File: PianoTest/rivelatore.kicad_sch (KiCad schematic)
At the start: 47 parts, among them J101 SMA preampl., J102 SMA shaper, Q101 BF862, Q102 BF862, U101 OPA4172ID, U102 ADS8326IDGKT, U103 TMP117AIDRVR

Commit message: PianoTest: discriminatore, latch e rilevatore di picco
Comparatore TLV3501 su SHAPER_OUT con soglia dal canale B del DAC61402
(partitore 22k/10k, BAT54S), latch 74LVC1G74 su GPA7 dell'MCP (ALERT#),
uscita HIT su TP e SMA. Rilevatore di picco OPA2365 + BAS416 + hold 1 nF
C0G prima dell'ADS8326, con reset da accesso SPI all'indirizzo 3 e
ponticello 0R per scavalcarlo. Trigger del LED dallo strobe dell'indirizzo 4.
Articolo: sezione 3.1 (formatore e acquisizione) aggiornata e ricompilata.
ERC 0.

Co-Authored-By: Claude Opus 5.5 (1M context) <noreply@anthropic.com>
Claude-Session: https://claude.ai/code/session_01J3krgWFTUEjwvCnwUp9cQn
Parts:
- added C108: 1nF C0G, Capacitor_SMD:C_0603_1608Metric, symbol Device:C
- added C118, C119, C120: 100nF, Capacitor_SMD:C_0603_1608Metric, symbol Device:C
- added D102, D103: BAS416, Diode_SMD:D_SOD-323, symbol Device:D
- added J103: SMA HIT, Connector_Coaxial:SMA_Amphenol_132134_Vertical, symbol Connector:Conn_Coaxial
- added Q103: BSS138, Package_TO_SOT_SMD:SOT-23, symbol PianoTest:BSS138
- added R130, R132: 1k, Resistor_SMD:R_0603_1608Metric, symbol Device:R
- added R131: 1M, Resistor_SMD:R_0603_1608Metric, symbol Device:R
- added R133: 10k, Resistor_SMD:R_0603_1608Metric, symbol Device:R
- added R134: 100k, Resistor_SMD:R_0603_1608Metric, symbol Device:R
- added R135, R136: 0R, Resistor_SMD:R_0603_1608Metric, symbol Device:R
- added R137: 100R, Resistor_SMD:R_0603_1608Metric, symbol Device:R
- added TP104: HIT, TestPoint:TestPoint_Pad_D1.0mm, symbol Connector:TestPoint
- added TP105: PK_OUT, TestPoint:TestPoint_Pad_D1.0mm, symbol Connector:TestPoint
- added U104: TLV3501AIDBVR, Package_TO_SOT_SMD:SOT-23-6, symbol PianoTest:TLV3501
- added U105: SN74LVC1G74DCUR, Package_SO:VSSOP-8_2.3x2mm_P0.5mm, symbol PianoTest:74LVC1G74
- added U106: OPA2365AIDR, Package_SO:SOIC-8_3.9x4.9mm_P1.27mm, symbol PianoTest:OPA2365
- added U107: SN74LVC1G04DBVR, Package_TO_SOT_SMD:SOT-23-5, symbol PianoTest:74LVC1G04
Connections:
- net +3V3: now also C118.1, C119.1, C120.1, U104.4 (V+), U105.2 (D), U105.7 (~{PRE}), U105.8 (VCC), U106.8 (V+), U107.5 (VCC)
- net GND: now also C108.2, C118.2, C119.2, C120.2, J103.2 (Ext), Q103.2 (S), R134.2, U104.2 (V-), U104.6 (SHDN), U105.4 (GND), U106.4 (V-), U107.3 (GND)
- net SHAPER_OUT: now also R130.1, R132.1, R136.1; no longer R106.1
- new net ADC_SRC: R106.1, R135.2, R136.2
- new net CMP_P: R130.2, R131.2, U104.3 (+IN)
- new net CS_Y3: U105.6 (~{CLR}), U107.2 (A)
- new net HIT: R131.1, R137.1, TP104.1, U104.5 (OUT), U105.1 (CLK)
- new net HIT_LATCH: U105.5 (Q)
- new net PK_A: D102.2 (A), D103.1 (K), U106.1 (OUTA)
- new net PK_FB: D103.2 (A), R133.2, U106.2 (-INA)
- new net PK_HOLD: C108.1, D102.1 (K), Q103.3 (D), U106.5 (+INB)
- new net PK_IN: R132.2, U106.3 (+INA)
- new net PK_OUT: R133.1, R135.1, TP105.1, U106.6 (-INB), U106.7 (OUTB)
- new net PK_RST: Q103.1 (G), R134.1, U107.4 (Y)
- new net SMA_HIT: J103.1 (In), R137.2
- new net VTH: U104.1 (-IN)
- no-connect marks 0 -> 2
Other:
- note added: "COMPARATORE E PICCO: TLV3501 (isteresi interna 6 mV) confronta SHAPER_OUT con VTH (DAC OUTB, partitore). HIT memorizzato da U105 -> HIT_LATCH -> MCP GPA7 -> ALERT#."
- note added: "Rilevatore di picco U106 (OPA2365 a 3V3, BAS416, hold 1 nF C0G) tra shaper e ADC. Reset di picco e latch: accesso SPI all'indirizzo 3 del piano (CS_Y3 basso). R135 diretto / R136 (DNP) scavalca il picco."

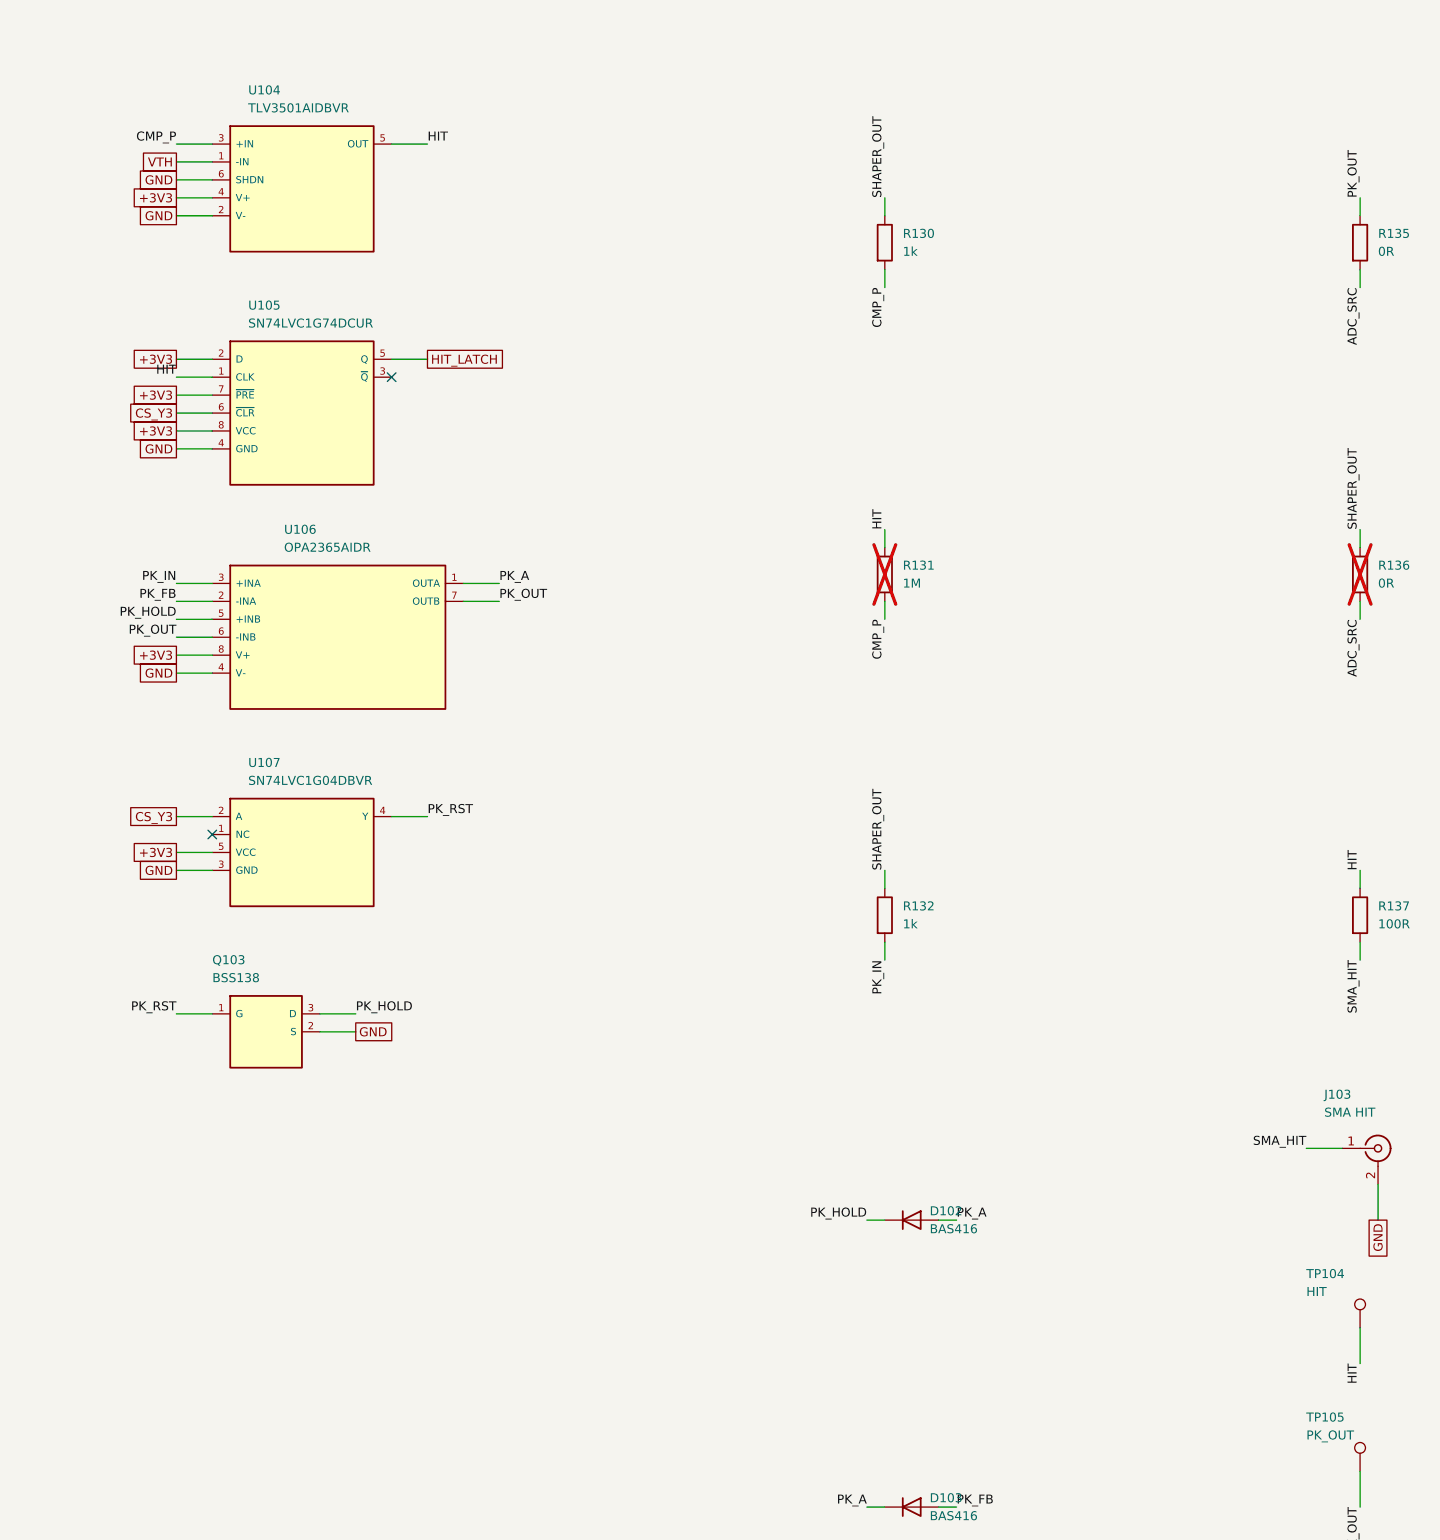
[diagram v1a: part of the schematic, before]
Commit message: Bus MIKILAB REV5.1: linea di coincidenza HIT# sul pin 28 del MAIN
Specifica: pin 28 (prima GND ridondante) = HIT#, open-drain attivo basso,
pull-up unico 4.7k sul master, impulso 100-200 ns per evento; logica di
coincidenza documentata (fronte marcato dal master, lettura dei latch).
PianoTest: HIT -> monostabile 74LVC1G123 (2k + 27 pF) -> 74LVC1G06 su
HIT#, passante J_IN -> J_OUT, ESD. ERC 0.
SchedaA133: J2 pin 28 -> PD4 (PD_EINT4), pull-up R336 4.7k, ESD su U307,
R337 0R DNP verso l'EXTINT del NEO-F10T. ERC 0, PDF rigenerato.
Documentazione bus della A133 e articolo (sezione bus e coincidenze)
aggiornati; corretta l'identita del primo piano (0).

Co-Authored-By: Claude Opus 5.5 (1M context) <noreply@anthropic.com>
Claude-Session: https://claude.ai/code/session_01J3krgWFTUEjwvCnwUp9cQn
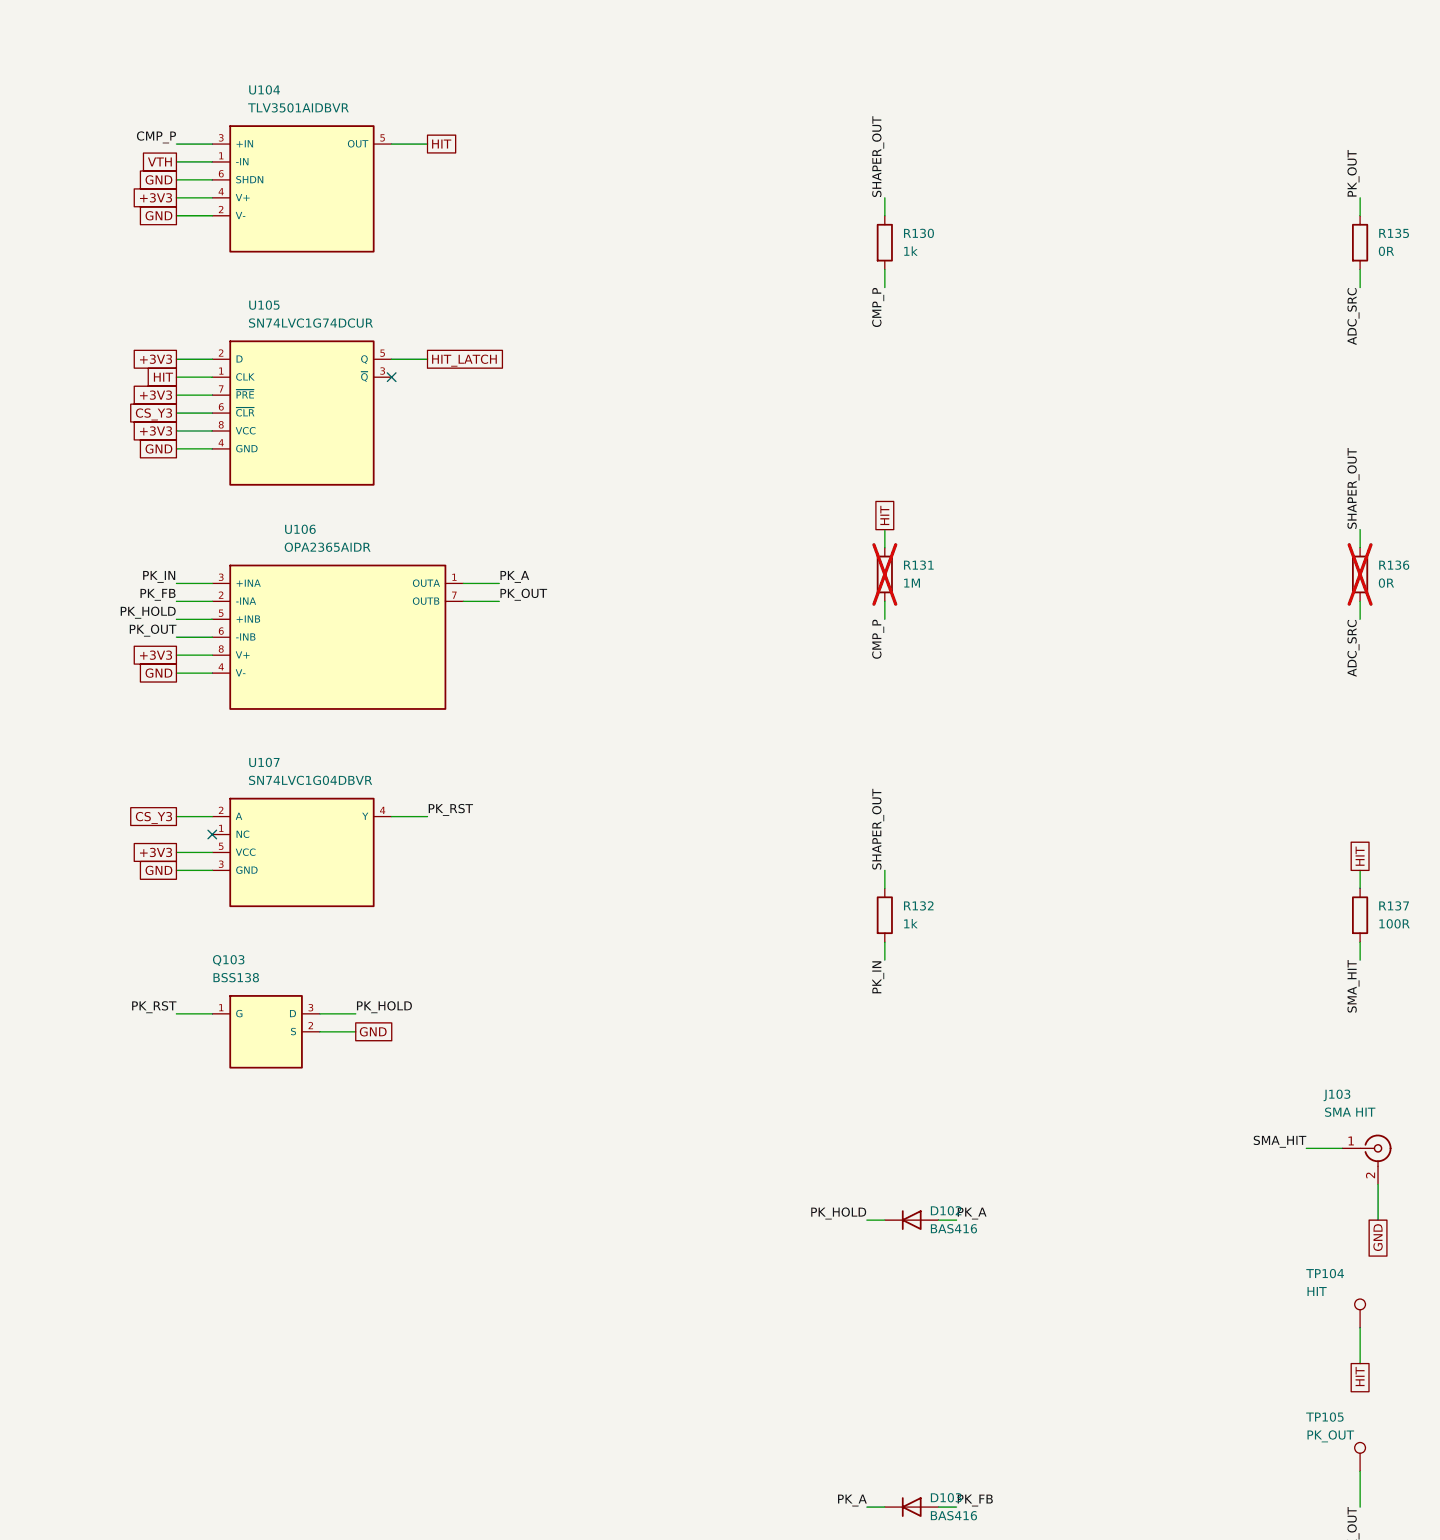
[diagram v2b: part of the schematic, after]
